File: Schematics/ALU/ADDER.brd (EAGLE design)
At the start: 73.9 x 68.2 mm, 44 parts

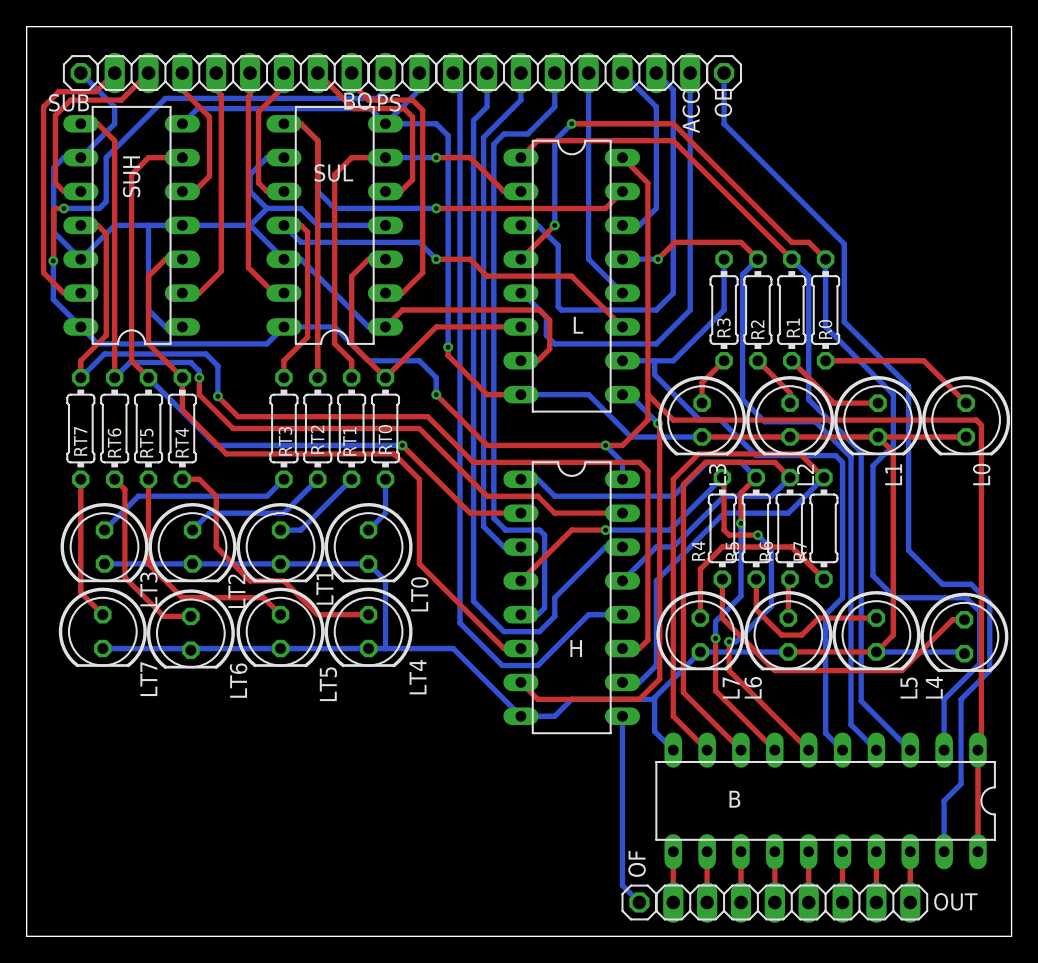
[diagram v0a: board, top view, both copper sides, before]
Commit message: Added backbone for ALU.
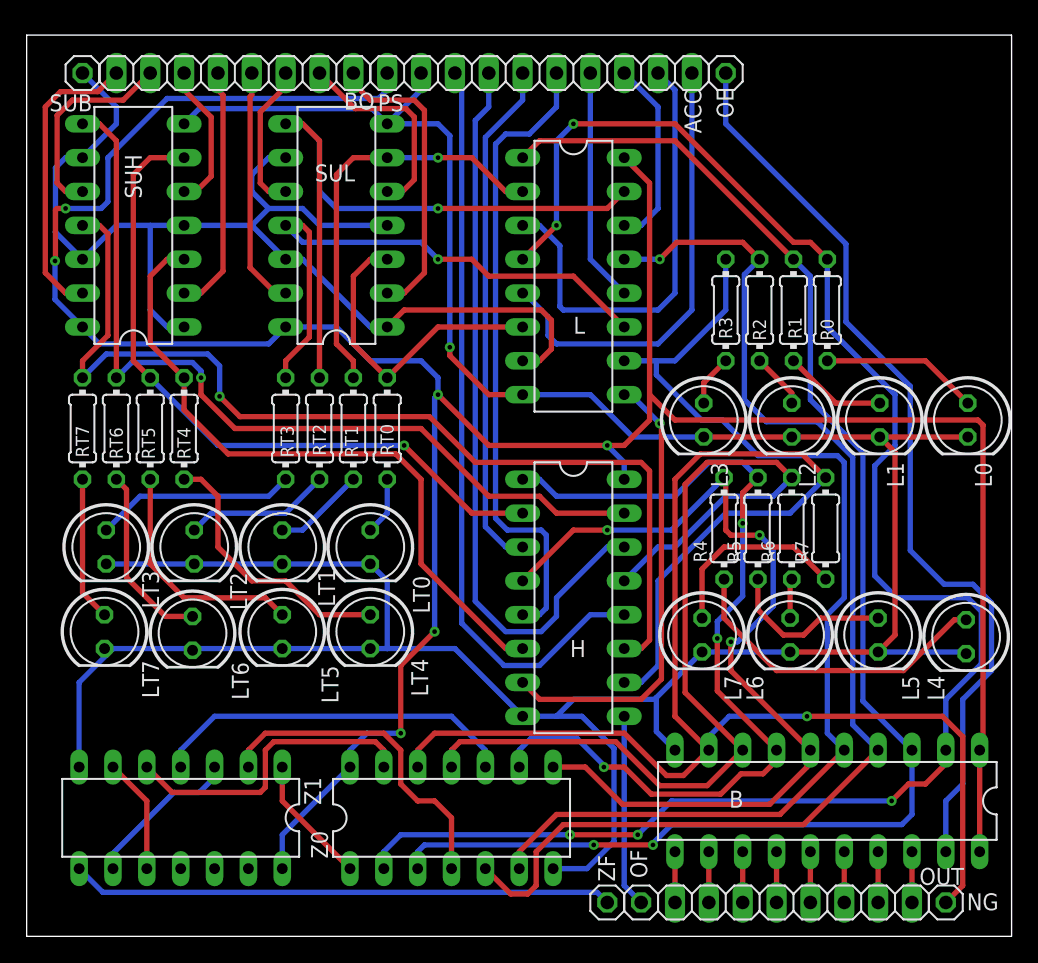
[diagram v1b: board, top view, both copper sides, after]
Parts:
- added NG, ZF: (no value), pinhead:1X01
- added Z0: 7402N, 74ttl-din:DIL14
- added Z1: 7408N, 74ttl-din:DIL14
- moved ACC 0.13 mm to (41.0, 64.8)
- moved H 0.13 mm to (41.0, 25.4)
- moved L 0.13 mm to (41.0, 49.5)
- moved L2 0.13 mm to (57.4, 38.7)
- moved L5 0.13 mm to (63.9, 22.6)
- moved L6 0.13 mm to (57.3, 22.6)
- moved L7 0.13 mm to (50.7, 22.6)
- moved OE 0.13 mm to (52.5, 64.8)
- moved OF 0.13 mm to (46.1, 2.54)
- moved PS 0.13 mm to (28.3, 64.8)
- moved R2 0.13 mm to (55.0, 47.0)
- moved R3 0.13 mm to (52.5, 47.0)
- moved R6 0.13 mm to (57.4, 30.6)
- moved R7 0.13 mm to (59.9, 30.6)
- moved RT3 0.13 mm to (19.4, 38.1)
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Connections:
- new net N$18: Z0.13, Z1.5
- new net N$20: Z0.10, Z1.4
- new net N$22: Z1.10, Z1.6
- new net N$26: Z1.3, Z1.9
- new net N$28: Z0.4, Z1.2
- new net N$30: Z0.1, Z1.1
- new net ZF: Z1.8, ZF.1
- net GND: now also Z0.7, Z1.7
- net S0: now also Z0.2
- net S1: now also Z0.3
- net S2: now also Z0.5
- net S3: now also Z0.6
- net S4: now also Z0.8
- net S5: now also Z0.9
- net S6: now also Z0.11
- net S7: now also NG.1, Z0.12
- net VCC: now also Z0.14, Z1.14
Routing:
- net S7: track 59.4 -> 119.4 mm, vias 0 -> 1
- net S0: track 82.1 -> 129.3 mm, vias 2 -> 5
- net S1: track 65.0 -> 109.5 mm, vias 0 -> 2
- net VCC: track 171.9 -> 213.8 mm, vias 4 -> 6
- net ZF: track 0.00 -> 40.7 mm
- net S2: track 54.9 -> 91.1 mm
- net S3: track 53.5 -> 82.3 mm
- net GND: track 201.2 -> 228.9 mm
- net N$20: track 0.00 -> 27.5 mm
- net S6: track 46.7 -> 72.5 mm
- net N$28: track 0.00 -> 25.0 mm
- net S5: track 43.3 -> 67.8 mm, vias 2 -> 3
- net N$18: track 0.00 -> 23.3 mm
- net S4: track 45.6 -> 68.4 mm
- net N$26: track 0.00 -> 11.9 mm
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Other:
- board size 73.9 x 68.2 mm -> 73.9 x 67.6 mm
